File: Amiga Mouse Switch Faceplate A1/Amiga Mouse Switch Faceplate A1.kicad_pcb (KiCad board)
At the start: 2 copper layers, 82.5 x 40.6 mm, 5 parts, among them M1 Mounting, M2 Mounting, M3 Mounting, M4 Mounting

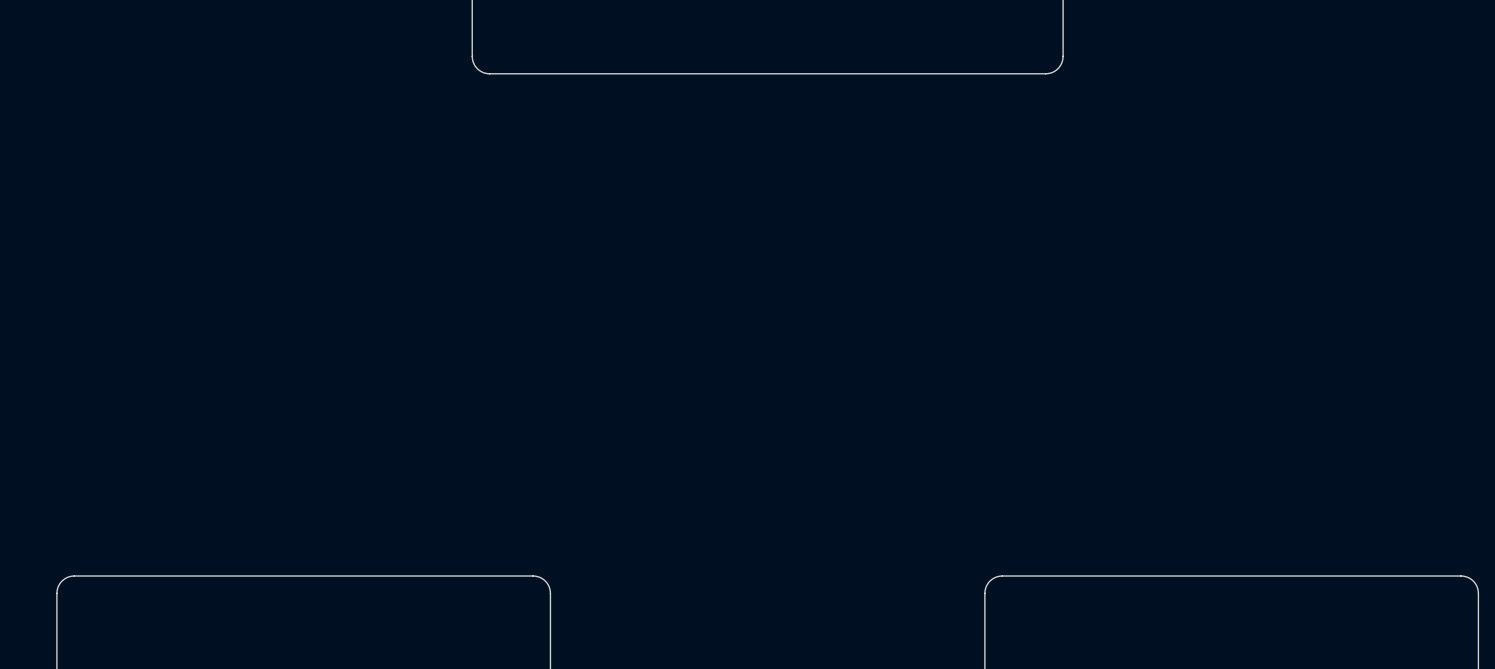
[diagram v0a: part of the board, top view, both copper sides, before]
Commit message: Added diode for lines that have pull-ups onboard
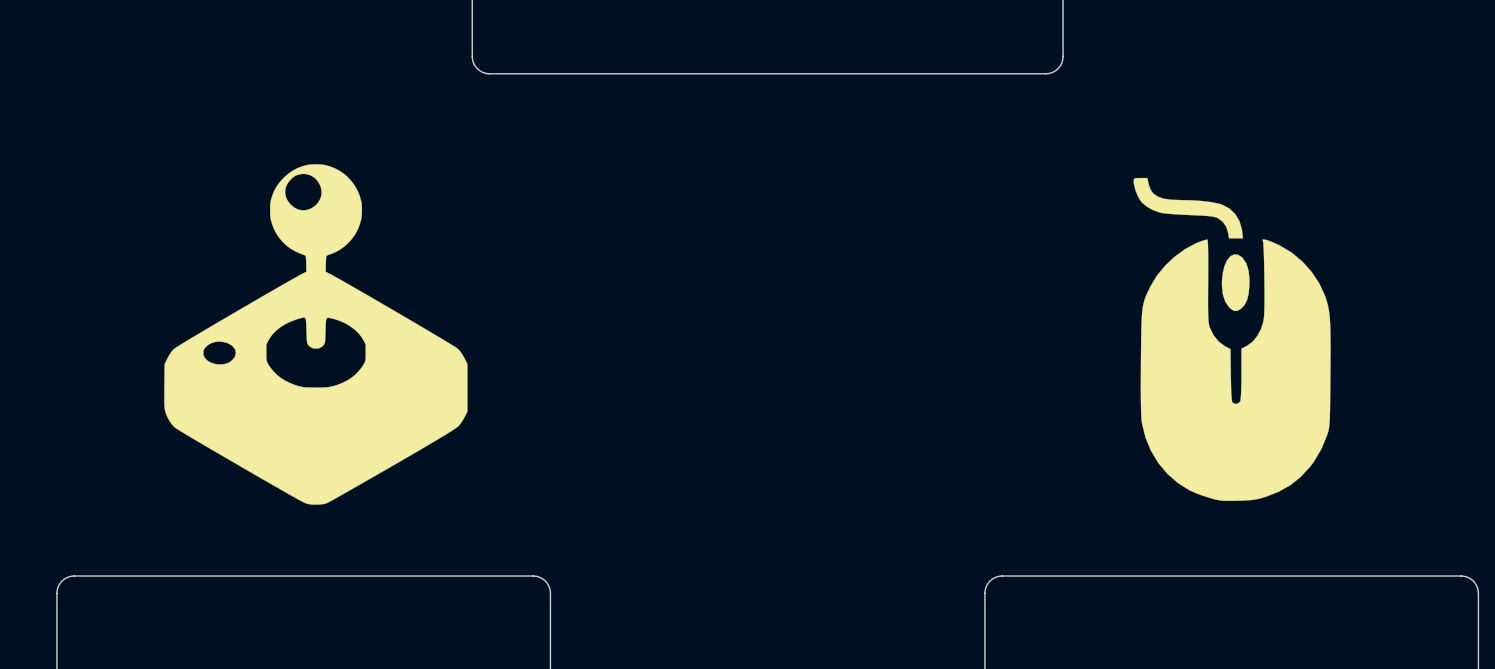
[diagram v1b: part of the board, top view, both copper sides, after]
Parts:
- added G***: LOGO, artwork:mouse, F.Cu at (156.8, 92.1)
- added G***: LOGO, artwork:joystick, F.Cu at (123.2, 91.4)
